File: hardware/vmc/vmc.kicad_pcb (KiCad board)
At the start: 2 copper layers, 63 x 29 mm, 35 parts, among them J1 Conn_01x05_Pin, J2 push button, J3 BUS, M1 Motor_DC, Q1 BSS123, U1 SHT31-DIS, U2 PIC18F05Q40, U3 DRV8832DGQR, U4 MCP2003B, U5 uA7805

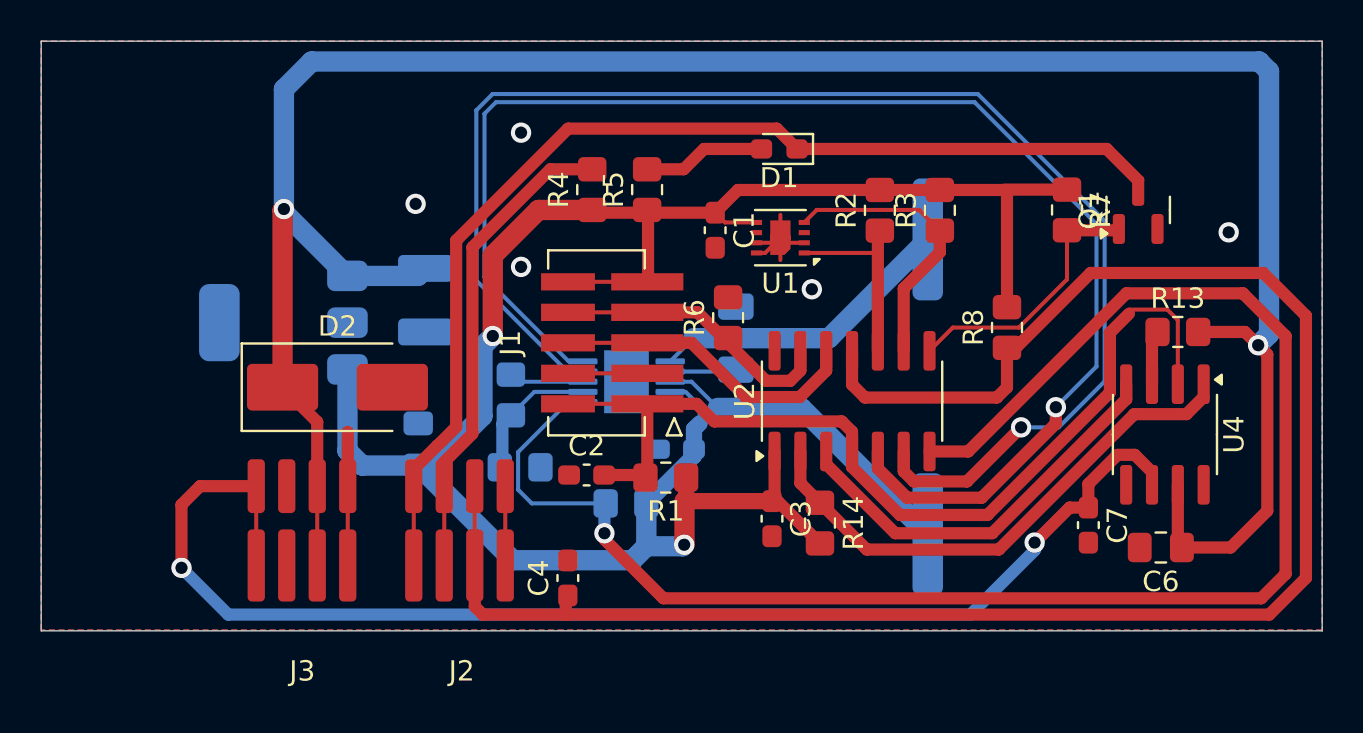
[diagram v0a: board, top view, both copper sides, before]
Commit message: vnc: Remplace le driver DRV8832DGQR (obsolete) par un MAX22201
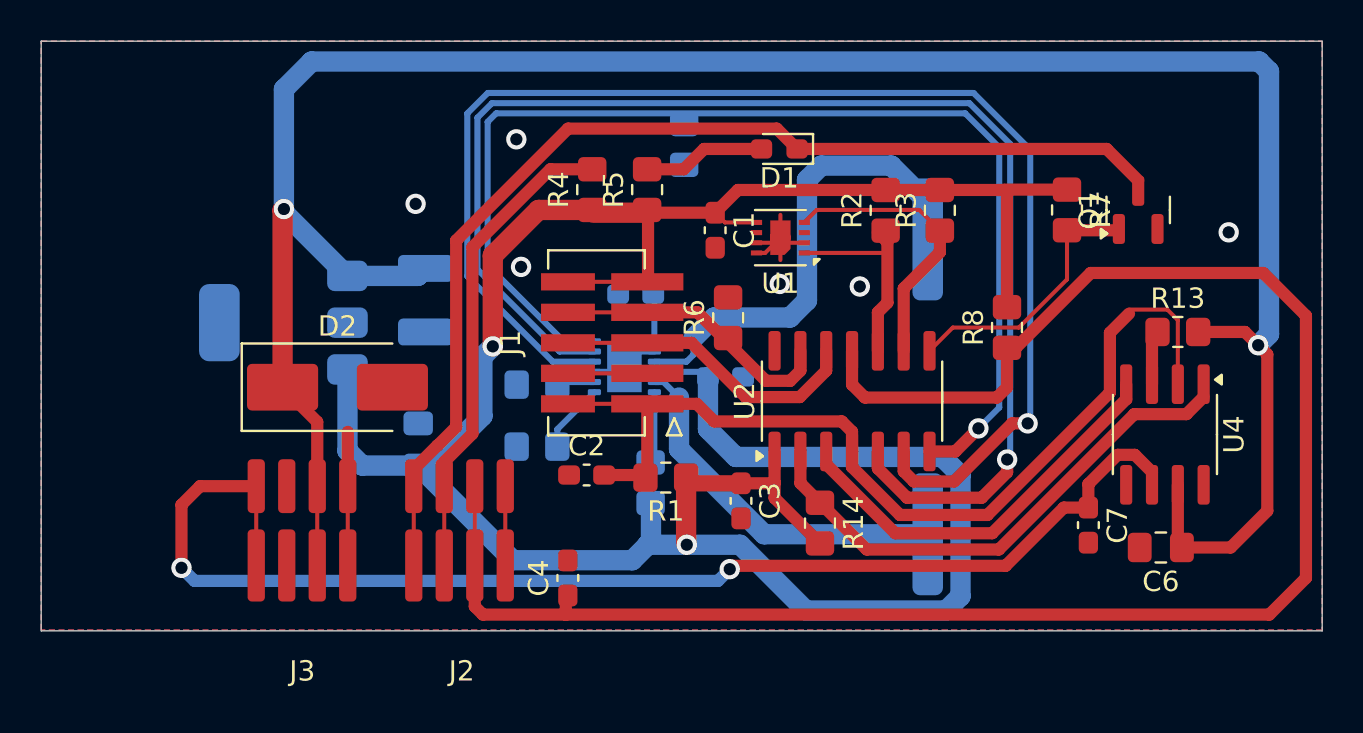
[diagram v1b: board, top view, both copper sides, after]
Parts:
- removed U3: DRV8832DGQR, Package_SO:MSOP-10-1EP_3x3mm_P0.5mm_EP2.2x3.1mm_Mask1.83x1.89mm
- added C10: 1µF, Capacitor_SMD:C_0603_1608Metric_Pad1.08x0.95mm_HandSolder, B.Cu at (129.2, 62.4)
- added U6: MAX22201, Package_DFN_QFN:Maxim_TDFN-12-1EP_3x3mm_P0.5mm_EP1.7x2.5mm, B.Cu at (128.7, 66.0)
- R10: value 0.68 -> 33K; footprint Resistor_SMD:R_1206_3216Metric_Pad1.30x1.75mm_HandSolder -> Resistor_SMD:R_0805_2012Metric_Pad1.20x1.40mm_HandSolder
- R12: value 10K -> 33K
- R9: value 10K -> 100K
- moved R11 15.0 mm to (131.6, 55.1)
- moved R10 10.0 mm to (124.4, 66.9), turned to 0 degrees
- moved R12 6.46 mm to (130.0, 71.7), turned to -90 degrees
- moved R9 5.19 mm to (124.4, 69.9)
- moved C5 4.30 mm to (133.7, 66.5), turned to 0 degrees
- moved C3 1.76 mm to (134.4, 72.6)
- moved R2 0.28 mm to (141.5, 58.3)
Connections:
- R11 pad 1: Net-(U3-VSET) -> GND
- R11 pad 2: Net-(U3-VREF) -> Net-(U2-RC3/CxIN3-)
- R12 pad 1: GND -> Net-(U6-~{FAULT})
- R12 pad 2: Net-(U3-VSET) -> +5V
- R9 pad 1: Net-(U2-RC3/CxIN3-) -> GND
- R9 pad 2: +5V -> Net-(U6-ILIM)
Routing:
- net +5V: track 103.1 -> 134.9 mm
- net Net-(U2-RC3/CxIN3-): track 80.8 -> 57.0 mm
- net Net-(M1--): track 15.1 -> 22.1 mm
- net Net-(U3-VSET): track 6.62 -> 0.00 mm
- net Net-(U3-VREF): track 3.61 -> 0.00 mm
- net Net-(U6-ILIM): track 0.00 -> 3.43 mm
- net Net-(U6-~{FAULT}): track 0.00 -> 3.27 mm
- net Net-(U2-RC4): track 70.3 -> 67.2 mm
- net Net-(U2-RC5): track 69.7 -> 66.7 mm
- net GND: track 19.9 -> 22.9 mm, vias 5 -> 6
- net Net-(M1-+): track 15.8 -> 18.0 mm
- net Net-(U6-V_{18}): track 0.00 -> 2.26 mm
- net /Lbus: track 64.2 -> 62.6 mm
- net Net-(U6-ROFF): track 3.13 -> 1.69 mm
- net Net-(U1-SDA): track 9.50 -> 10.3 mm

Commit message: vmc: swap button/LED pins to limit damage on accidental connect to LIN bus. Name remaining connector signals
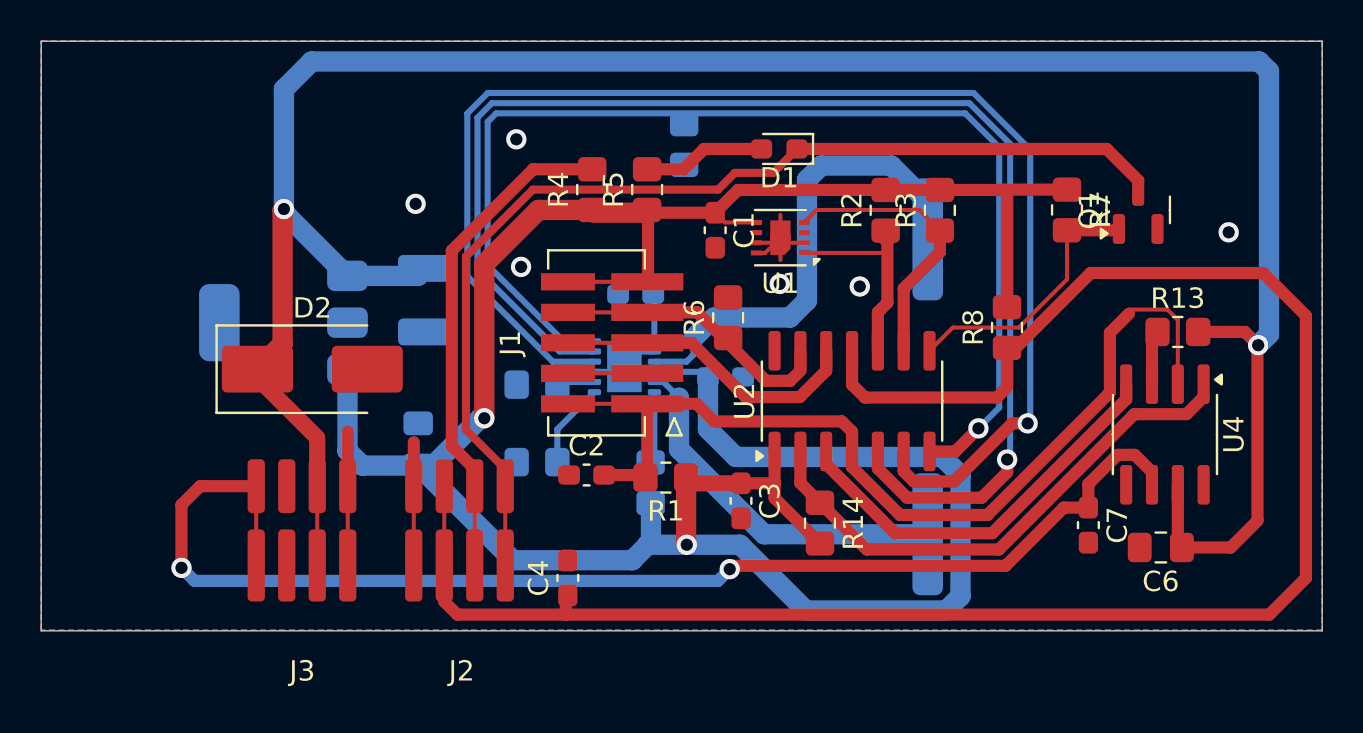
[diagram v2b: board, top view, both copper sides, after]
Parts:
- moved D2 1.52 mm to (113.3, 66.1)
- moved R9 0.76 mm to (124.4, 70.7)
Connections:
- D1 pad 1: Net-(D1-K) -> /LED-
- J2 pad 1: Net-(D1-K) -> GND
- J2 pad 2: Net-(J2-Pin_2) -> /~{PUSH}
- J2 pad 3: /~{PUSH} -> /LED+
- J2 pad 4: GND -> /LED-
- Q1 pad 3: Net-(D1-K) -> /LED-
- R4 pad 2: Net-(J2-Pin_2) -> /LED+
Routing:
- net Net-(D1-K): track 52.9 -> 0.00 mm
- net /LED-: track 0.00 -> 51.0 mm
- net Net-(J2-Pin_2): track 23.7 -> 0.00 mm
- net /LED+: track 0.00 -> 23.7 mm
- net GND: track 22.9 -> 25.1 mm
- net /~{PUSH}: track 90.2 -> 91.6 mm
- net Net-(U6-ILIM): track 3.43 -> 4.19 mm

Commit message: Alimente le driver max22201 en 12V; le courant moteur est limité par le driver en PWM et cela permet de tirer un peu moins sur l'alim (et le régulateur 5V)
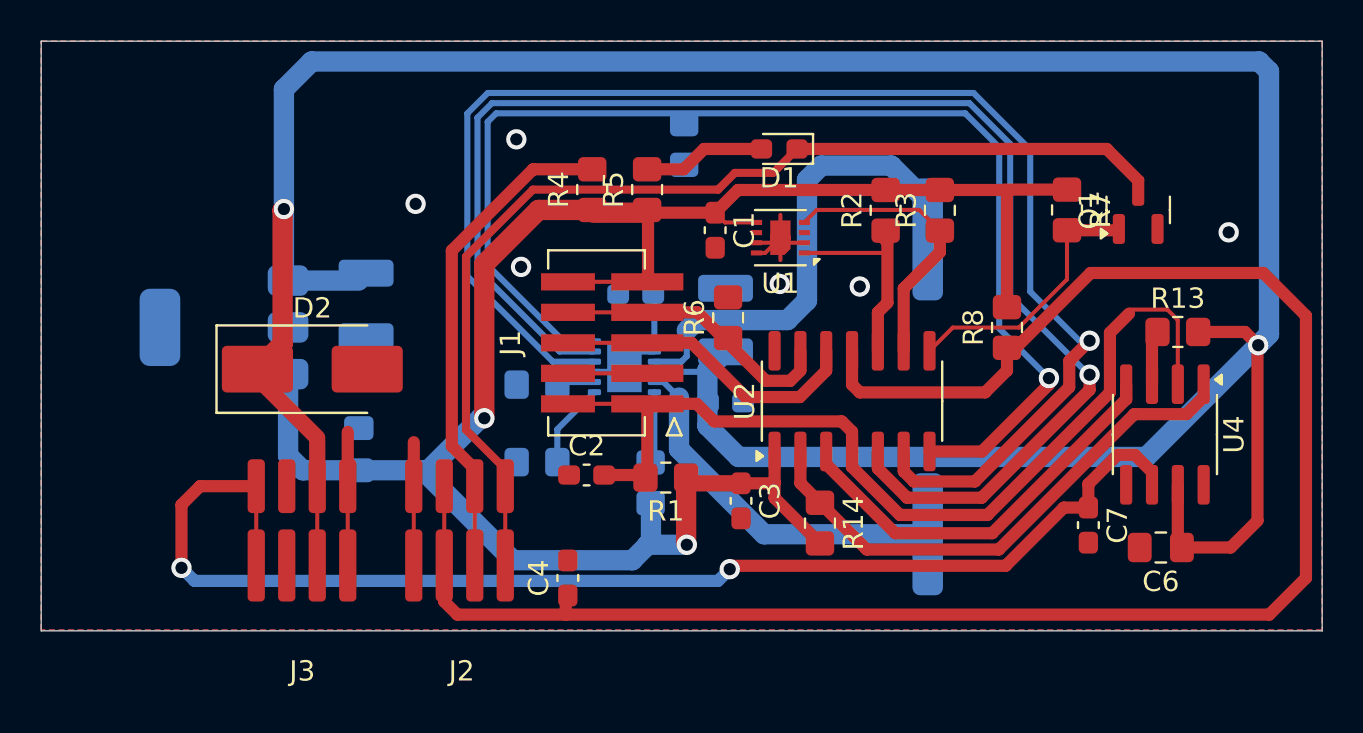
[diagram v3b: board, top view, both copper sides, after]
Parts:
- added C11: 10uF, Capacitor_SMD:C_1210_3225Metric_Pad1.33x2.70mm_HandSolder, B.Cu at (133.7, 63.7)
- M1: value Motor_DC -> F130
- moved C9 2.93 mm to (115.6, 70.1)
- moved C8 2.93 mm to (116.0, 63.0)
- moved U5 2.93 mm to (109.0, 64.1)
- moved C5 1.27 mm to (133.7, 67.8)
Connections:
- C5 pad 1: +5V -> /+12V
- U6 pad 10: +5V -> /+12V
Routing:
- net +5V: track 135.1 -> 98.4 mm
- net /+12V: track 114.8 -> 149.7 mm
- net Net-(U2-RC5): track 66.7 -> 70.0 mm
- net Net-(U2-RC4): track 67.2 -> 70.1 mm
- net Net-(U2-RC3/CxIN3-): track 57.0 -> 59.8 mm
- net /~{PUSH}: track 91.6 -> 90.9 mm

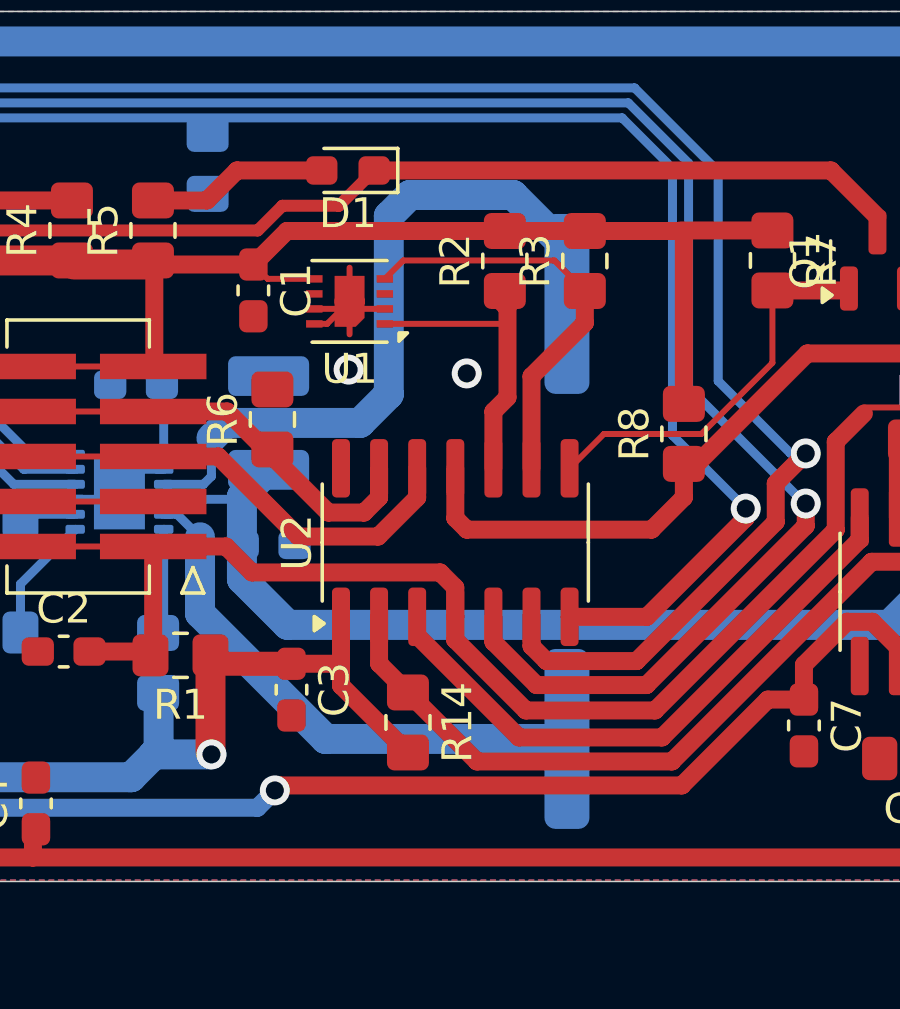
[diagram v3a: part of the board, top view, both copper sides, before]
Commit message: vmc: adjust motor position
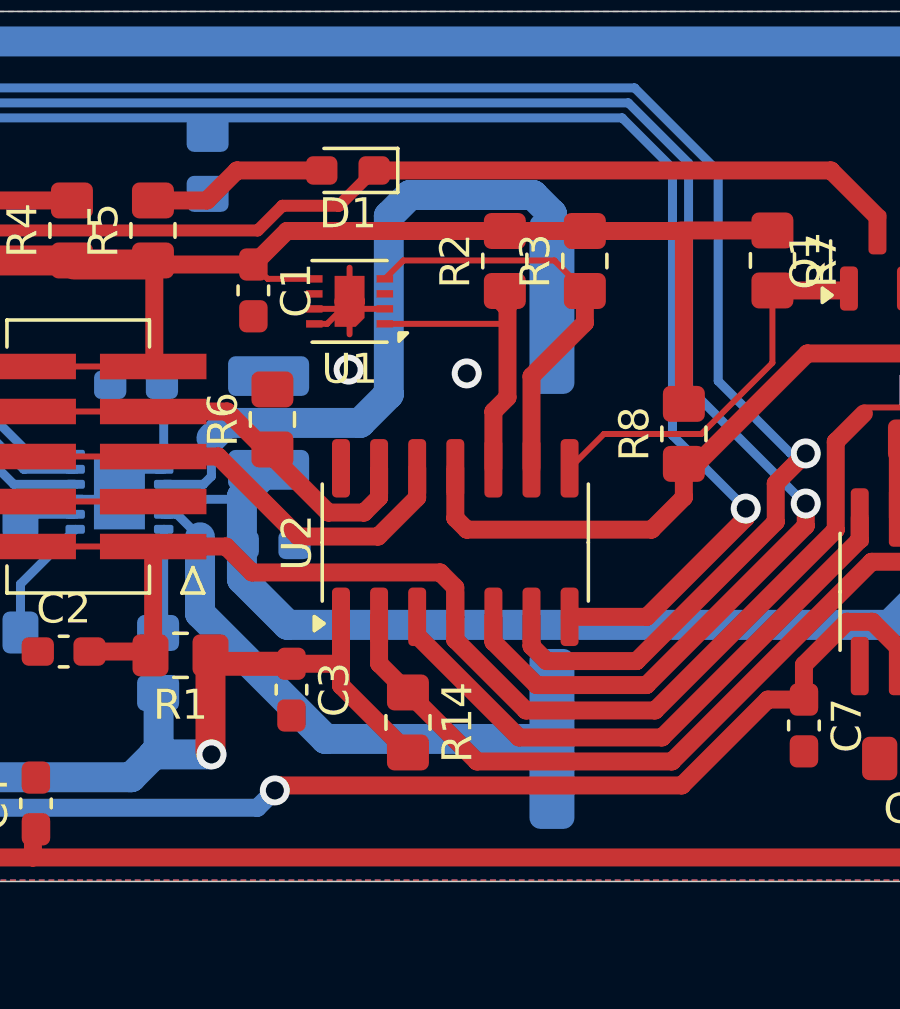
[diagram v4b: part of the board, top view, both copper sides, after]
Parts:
- moved M1 0.50 mm to (164.7, 67.0)
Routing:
- net Net-(M1--): track 22.4 -> 24.4 mm
- net Net-(M1-+): track 18.0 -> 17.5 mm

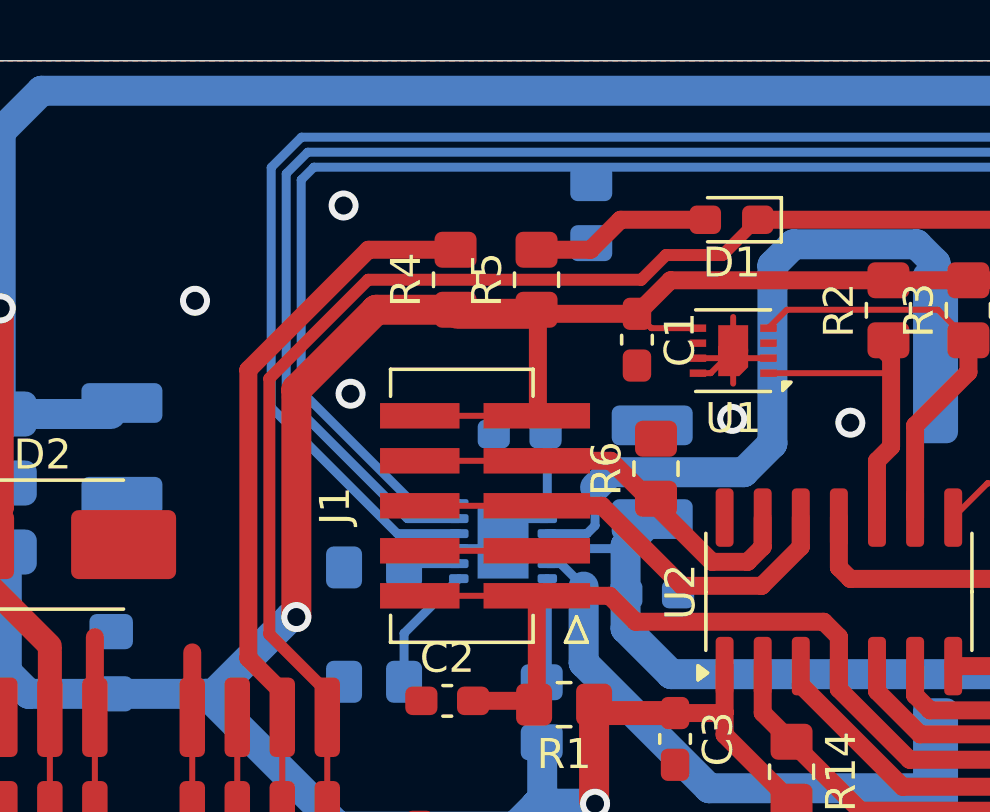
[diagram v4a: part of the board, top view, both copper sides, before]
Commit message: vmc: update ICSP connector to match ventil
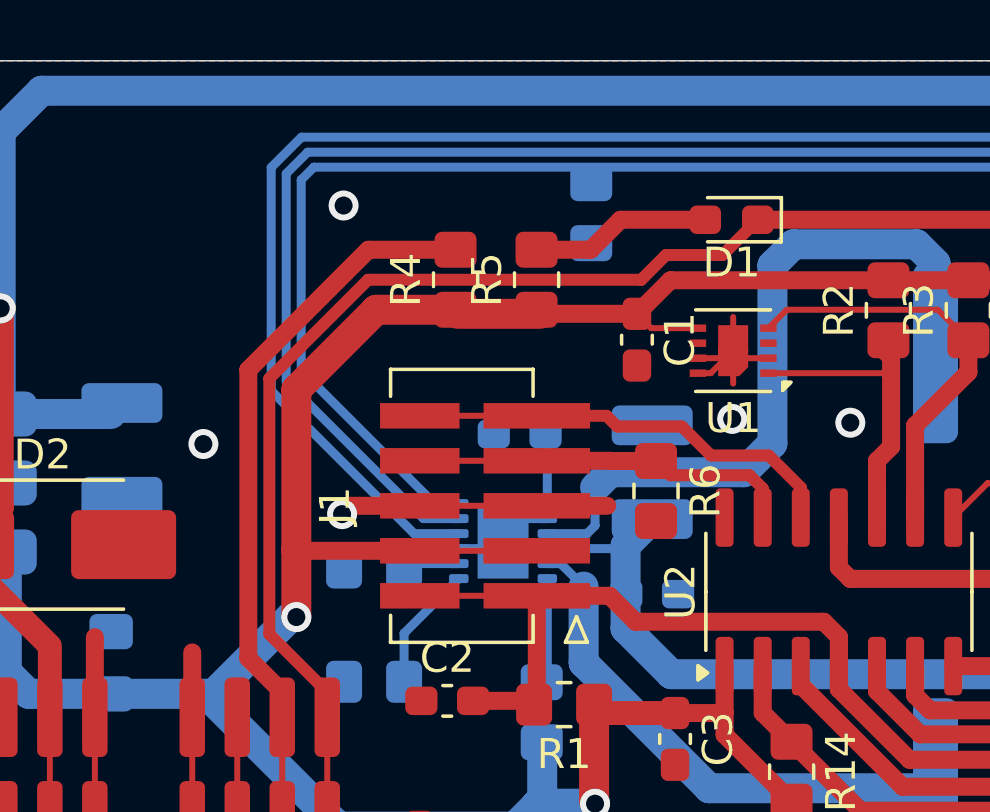
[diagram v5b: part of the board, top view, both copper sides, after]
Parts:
- moved R6 0.74 mm to (133.8, 64.3), turned to -90 degrees
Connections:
- J1 pad 2: GND -> +5V
- J1 pad 3: /PGC -> GND
- J1 pad 5: +5V -> /PGC
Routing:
- net GND: track 25.1 -> 29.8 mm
- net /PGD: track 14.0 -> 12.8 mm
- net +5V: track 98.4 -> 99.2 mm
- net /PGC: track 15.3 -> 14.7 mm

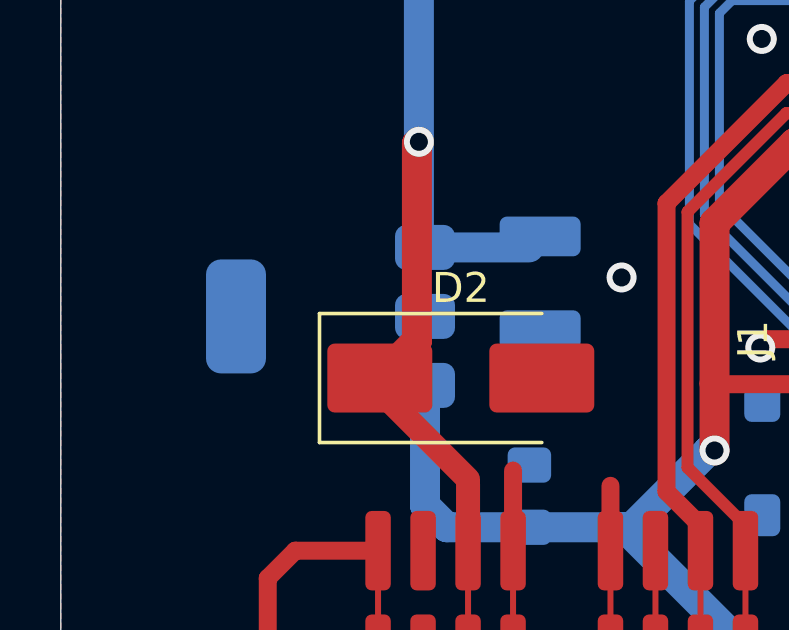
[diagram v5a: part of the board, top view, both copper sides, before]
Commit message: ventil, vmc: switch 7805 to a less expensive package
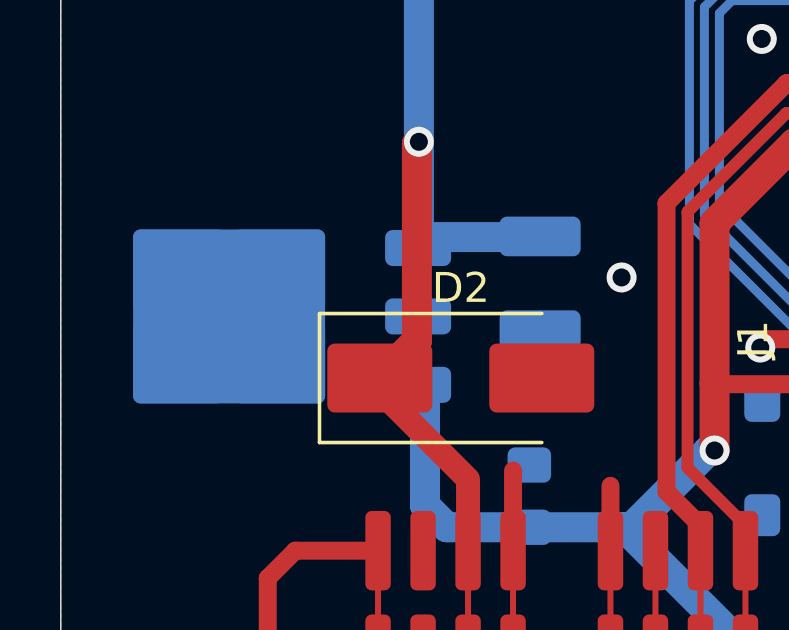
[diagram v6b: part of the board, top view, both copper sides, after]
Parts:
- U5: footprint Package_TO_SOT_SMD:SOT-223-3_TabPin2 -> Package_TO_SOT_SMD:TO-252-3_TabPin2
- moved U5 2.12 mm to (106.9, 64.1)
